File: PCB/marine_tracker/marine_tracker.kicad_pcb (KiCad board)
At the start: 4 copper layers, 83.9 x 40.3 mm, 64 parts, among them J1 Screw_Terminal_01x02, J2 Conn_ARM_JTAG_SWD_10, J3 USB_C_Receptacle_USB2.0_16P, J4 BM04B-GHS-TBT, J5 Conn_01x08_Pin, J6 Conn_Coaxial, SW2 SW_Push, U1 STM32U575RGT6, U2 SHT40, U3 MCP73833-xxx-UN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

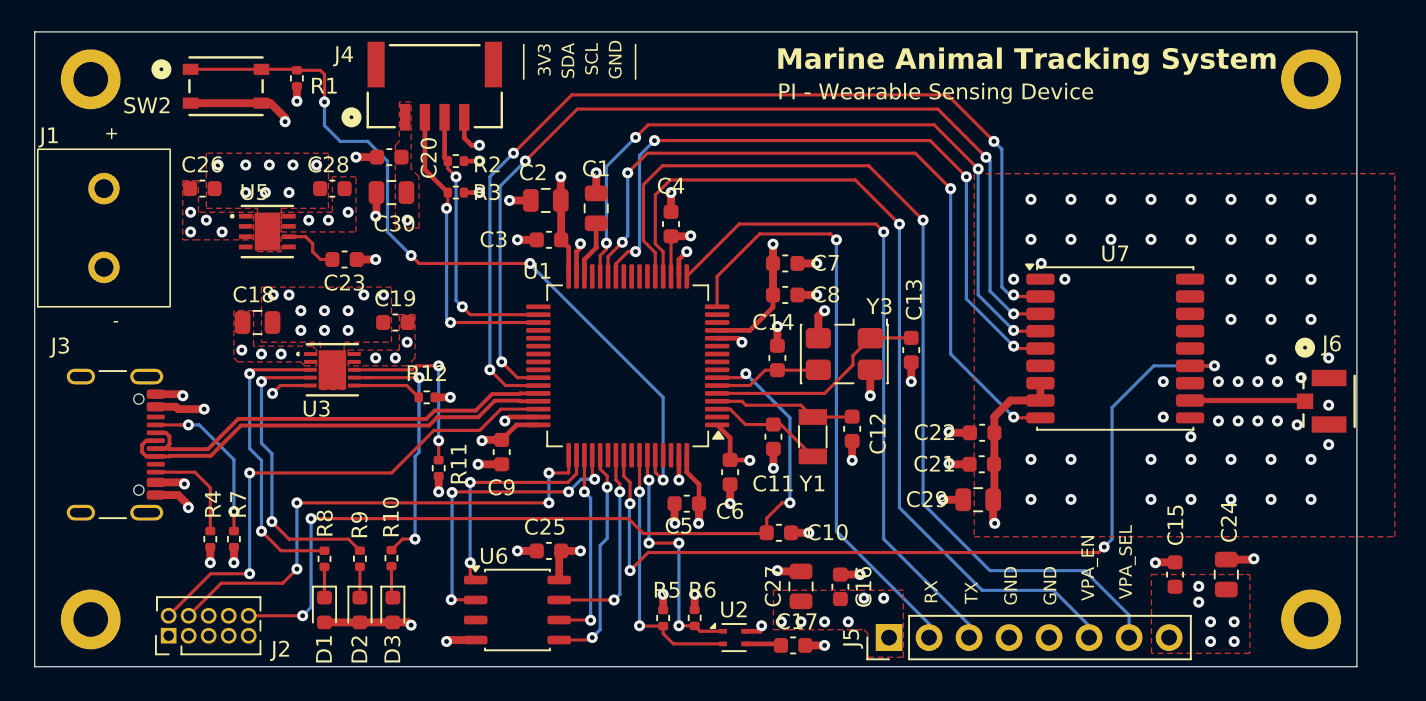
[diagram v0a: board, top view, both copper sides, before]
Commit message: adding testpoint
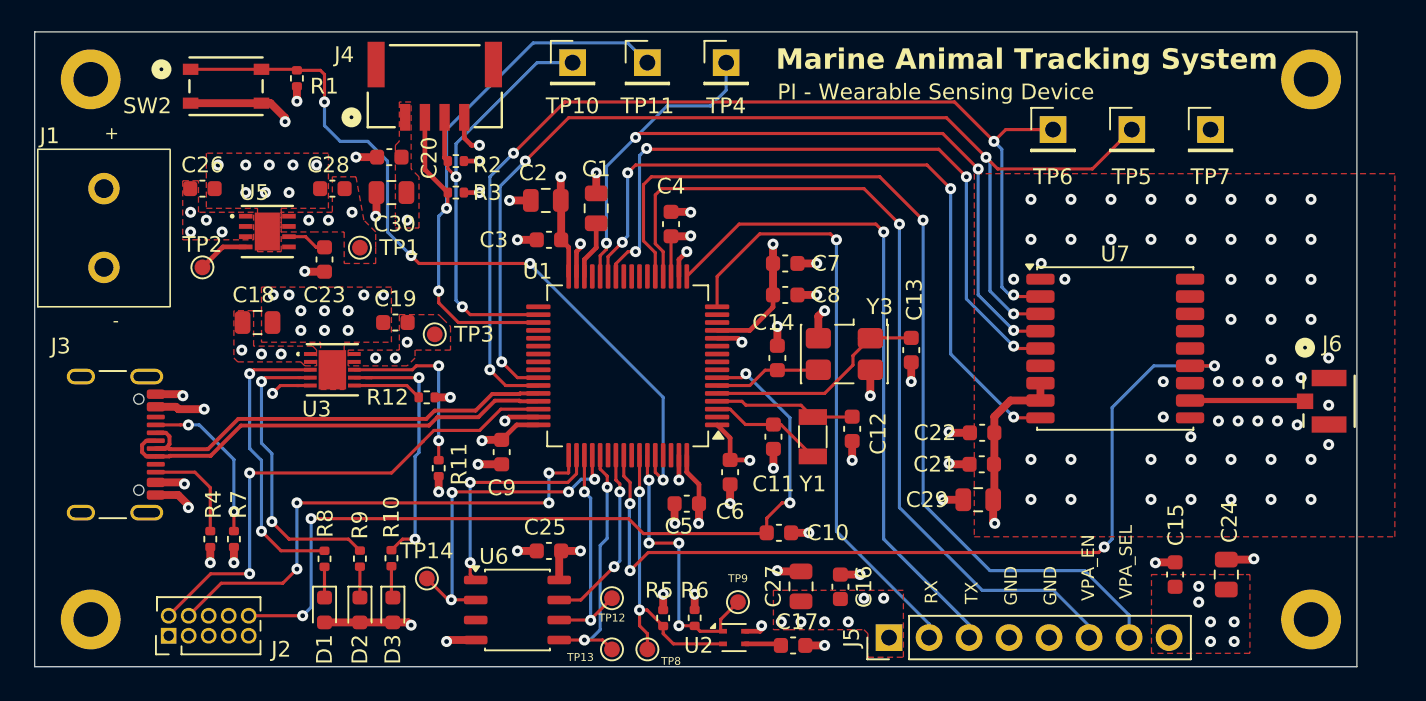
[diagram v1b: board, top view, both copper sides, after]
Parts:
- added TP1: TestPoint, TestPoint:TestPoint_Pad_D1.0mm, F.Cu at (59.0, 78.0)
- added TP10: TestPoint, Connector_PinHeader_2.54mm:PinHeader_1x01_P2.54mm_Vertical, F.Cu at (72.5, 66.2)
- added TP11: TestPoint, Connector_PinHeader_2.54mm:PinHeader_1x01_P2.54mm_Vertical, F.Cu at (77.2, 66.2)
- added TP12: TestPoint, TestPoint:TestPoint_Pad_D1.0mm, F.Cu at (75.0, 100.2)
- added TP13: TestPoint, TestPoint:TestPoint_Pad_D1.0mm, F.Cu at (75.0, 103.5)
- added TP14: TestPoint, TestPoint:TestPoint_Pad_D1.0mm, F.Cu at (63.2, 99.0)
- added TP2: TestPoint, TestPoint:TestPoint_Pad_D1.0mm, F.Cu at (49.0, 79.2)
- added TP3: TestPoint, TestPoint:TestPoint_Pad_D1.0mm, F.Cu at (63.8, 83.5)
- added TP4: TestPoint, Connector_PinHeader_2.54mm:PinHeader_1x01_P2.54mm_Vertical, F.Cu at (82.2, 66.2)
- added TP5: TestPoint, Connector_PinHeader_2.54mm:PinHeader_1x01_P2.54mm_Vertical, F.Cu at (108.0, 70.5)
- added TP6: TestPoint, Connector_PinHeader_2.54mm:PinHeader_1x01_P2.54mm_Vertical, F.Cu at (103.0, 70.5)
- added TP7: TestPoint, Connector_PinHeader_2.54mm:PinHeader_1x01_P2.54mm_Vertical, F.Cu at (113.0, 70.5)
- added TP8: TestPoint, TestPoint:TestPoint_Pad_D1.0mm, F.Cu at (77.2, 103.5)
- added TP9: TestPoint, TestPoint:TestPoint_Pad_D1.0mm, F.Cu at (83.0, 100.5)
- moved C23 1.27 mm to (56.8, 78.8), turned to -90 degrees
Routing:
- net PRES_I2C2_SDA: track 19.3 -> 40.0 mm
- net PRES_I2C2_SCL: track 17.5 -> 29.2 mm
- net GPS_RXD: track 60.5 -> 70.6 mm
- net GPS_PULSE: track 45.9 -> 54.2 mm
- net GPS_TXD: track 63.3 -> 67.0 mm
- net GND: track 64.5 -> 67.9 mm
- net SHT_SDA: track 15.7 -> 18.1 mm
- net SHT_SCL: track 16.9 -> 19.0 mm
- net MEM_SPI3_MISO: track 19.4 -> 21.5 mm
- net MEM_SPI3_MOSI: track 14.5 -> 16.4 mm
- net MEM_SPI3_SCK: track 12.8 -> 14.8 mm
- net MEM_HOLD: track 12.9 -> 11.7 mm
- net Net-(U5-CDELAY): track 3.65 -> 2.54 mm
- net GPS_N_RST: track 46.9 -> 46.3 mm
- net SAT_VPA_SEL: track 61.2 -> 60.7 mm
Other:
- board text removed: "3V3"
- board text removed: "SCL"
- board text removed: "SDA"
